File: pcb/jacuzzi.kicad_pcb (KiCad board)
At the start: 2 copper layers, 130 x 100 mm, 94 parts, among them J1 Conn_01x03, J10 Conn_01x02, J11 Conn_01x03, J12 Conn_01x03, J13 LOGO, J14 LOGO, J15 LOGO, J16 LOGO, J19 Conn_01x03, J2 Conn_01x03, J3 Conn_01x03, J4 Conn_02x02_Counter_Clockwise_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, J5 Conn_01x03, J6 Conn_01x03, J7 Conn_01x02, J8 Conn_01x06, J9 USB_C_Receptacle_PowerOnly_6P, K1 SRD-05VDC, Q1 MMBT3904, Q2 MMBT3904, Q3 MMBT3904, Q4 IRF4905STRLPBF, Q5 MMBT3904, Q6 IRF4905STRLPBF, Q7 MMBT3904, U1 LM2575-3.3BU, U2 LM2575-5.0BU, U3 ESP32-DEVKITC-32U, U4 DM-OLED096-636

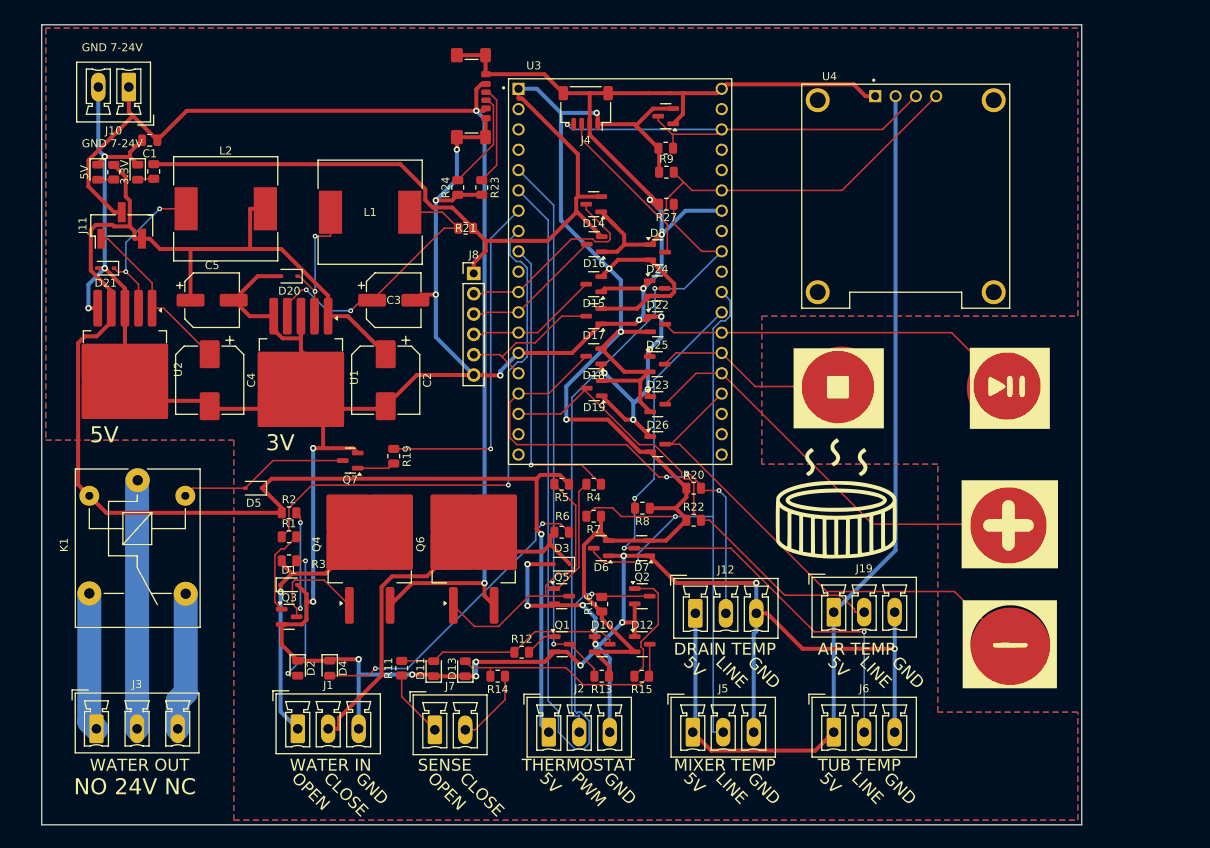
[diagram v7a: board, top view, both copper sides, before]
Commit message: issue with usb change the footprint
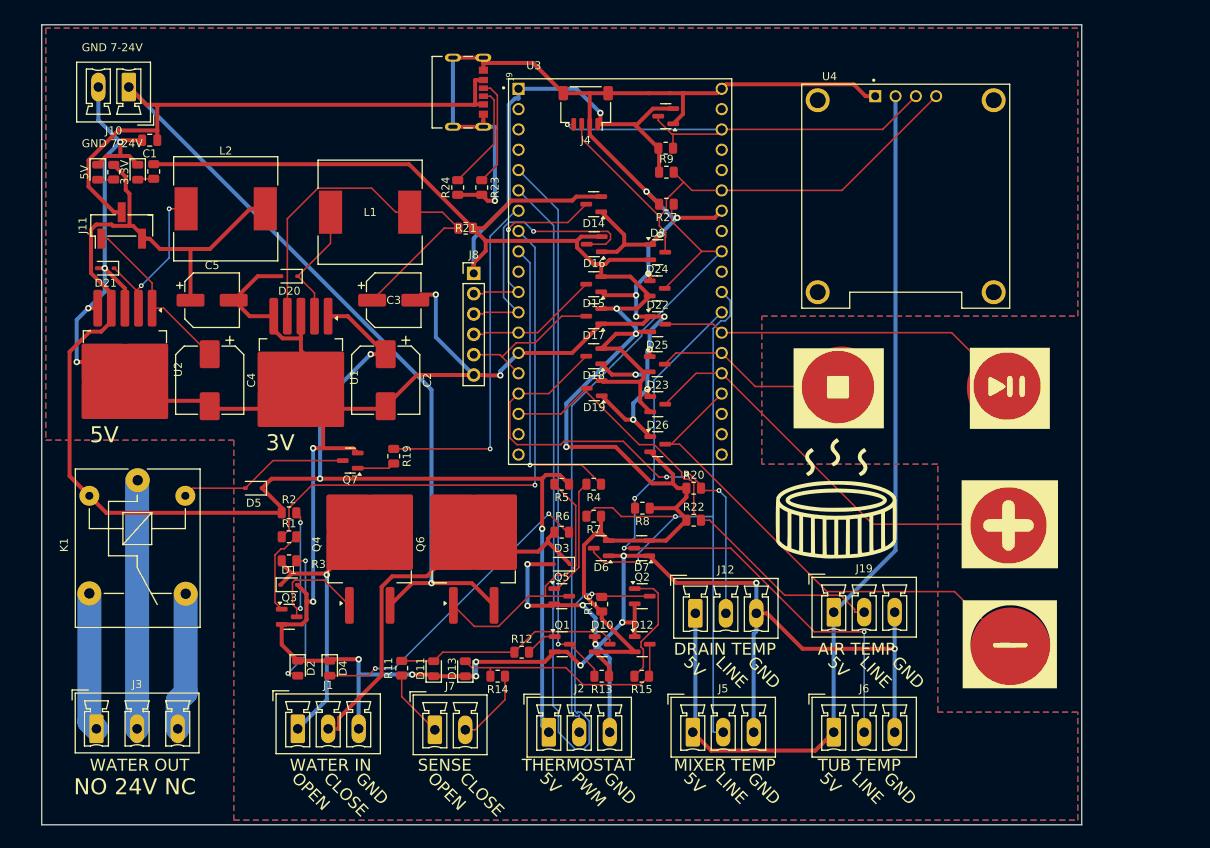
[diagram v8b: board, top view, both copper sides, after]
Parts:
- J9: value USB_C_Receptacle_PowerOnly_6P -> UJC-HP-3-SMT-TR; footprint Connector_USB:USB_C_Receptacle_GCT_USB4135-GF-A_6P_TopMnt_Horizontal -> UJC-HP-3-SMT-TR:CUI_UJC-HP-3-SMT-TR
- moved J9 2.75 mm to (129.2, 51.0)
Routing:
- net VS: track 147.4 -> 165.7 mm, vias 2 -> 1
- net /GPIO_ADC2: track 17.7 -> 35.2 mm, vias 0 -> 1
- net Net-(U1-FB): track 35.9 -> 51.7 mm, vias 2 -> 0
- net +3.3V: track 280.2 -> 284.0 mm
- net GND: track 598.8 -> 602.1 mm, vias 31 -> 33
- net /GPIO_Servo: track 82.0 -> 85.3 mm, vias 1 -> 0
- net +5V: track 323.3 -> 326.1 mm, vias 1 -> 3
- net Net-(D20-K): track 17.9 -> 15.6 mm, vias 2 -> 0
- net /BallValveOpen: track 48.4 -> 50.5 mm
- net /GPIO_BallValveOpen: track 67.3 -> 68.5 mm
- net Net-(J9-CC2): track 12.4 -> 13.5 mm
- net Net-(J9-CC1): track 12.5 -> 13.5 mm
- net /GPIO_ADC1: track 25.8 -> 25.1 mm, vias 0 -> 1
- net Net-(D21-K): track 19.8 -> 20.3 mm
